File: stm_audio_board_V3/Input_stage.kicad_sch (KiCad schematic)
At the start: 92 parts, among them U4 OP275

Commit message: minor changes
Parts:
- removed D4 (x4), D6 (x4), D8 (x4), D9 (x4): BAT42W-V, Diode_SMD:D_SOD-123, symbol Diode:BAT42W-V

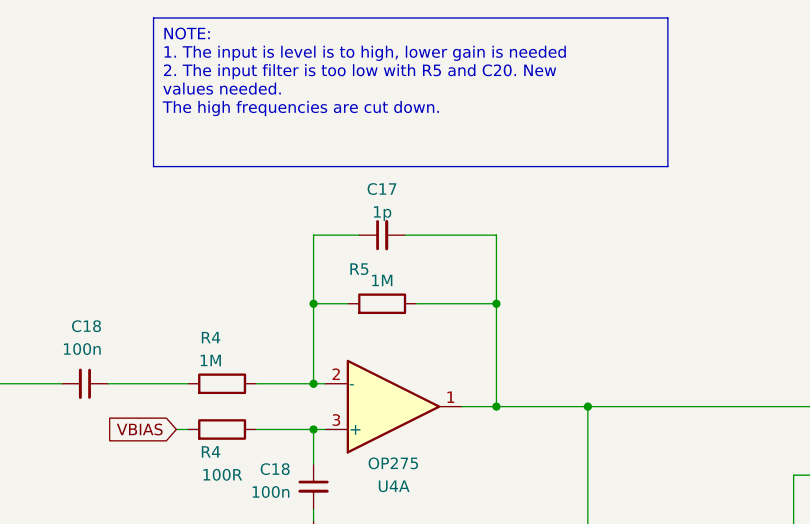
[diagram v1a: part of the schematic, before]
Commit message: Analog power and SDRAm routing reworked
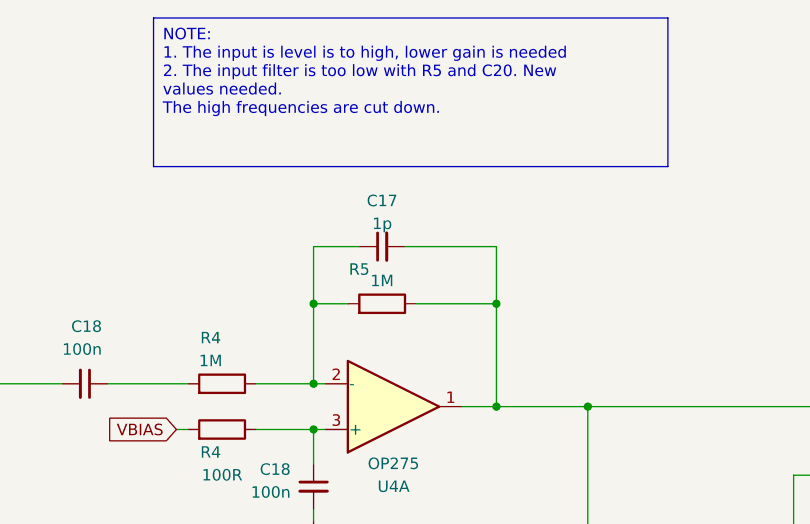
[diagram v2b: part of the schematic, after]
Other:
- moved on the sheet: C17
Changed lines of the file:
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@@
     (stroke (width 0) (type default))
   )
-  (wire (pts (xy 110.49 53.34) (xy 105.41 53.34))
+  (wire (pts (xy 110.49 54.61) (xy 105.41 54.61))
     (stroke (width 0) (type default))
   )
@@
     (stroke (width 0) (type default))
   )
-  (wire (pts (xy 115.57 53.34) (xy 125.73 53.34))
+  (wire (pts (xy 115.57 54.61) (xy 125.73 54.61))
     (stroke (width 0) (type default))
   )
@@
     (stroke (width 0) (type default))
   )
-  (wire (pts (xy 125.73 60.96) (xy 125.73 53.34))
+  (wire (pts (xy 125.73 54.61) (xy 125.73 60.96))
     (stroke (width 0) (type default))
   )
@@
     (stroke (width 0) (type default))
   )
-  (wire (pts (xy 105.41 60.96) (xy 105.41 53.34))
+  (wire (pts (xy 105.41 54.61) (xy 105.41 60.96))
     (stroke (width 0) (type default))
   )
@@
     )
   )
-  (symbol (lib_id "Device:C_Small") (at 113.03 53.34 90) (mirror x) (unit 1)
-    (in_bom yes) (on_board yes) (dnp no)
-    (property "Reference" "C17" (at 113.0363 48.26 90)
-      (effects (font (size 1.27 1.27)))
-    )
-    (property "Value" "1p" (at 113.0363 50.8 90)
-      (effects (font (size 1.27 1.27)))
-    )
-    (property "Footprint" "Capacitor_SMD:C_0603_1608Metric" (at 113.03 53.34 0)
-      (effects (font (size 1.27 1.27)) hide)
-    )
-    (property "Datasheet" "~" (at 113.03 53.34 0)
-      (effects (font (size 1.27 1.27)) hide)
-    )
+  (symbol (lib_id "Device:C_Small") (at 113.03 54.61 90) (mirror x) (unit 1)
+    (in_bom yes) (on_board yes) (dnp no)
+    (property "Reference" "C17" (at 113.0363 49.53 90)
+      (effects (font (size 1.27 1.27)))
+    )
+    (property "Value" "1p" (at 113.0363 52.07 90)
+      (effects (font (size 1.27 1.27)))
+    )
+    (property "Footprint" "Capacitor_SMD:C_0603_1608Metric" (at 113.03 54.61 0)
+      (effects (font (size 1.27 1.27)) hide)
+    )
+    (property "Datasheet" "~" (at 113.03 54.61 0)
+      (effects (font (size 1.27 1.27)) hide)
+    )

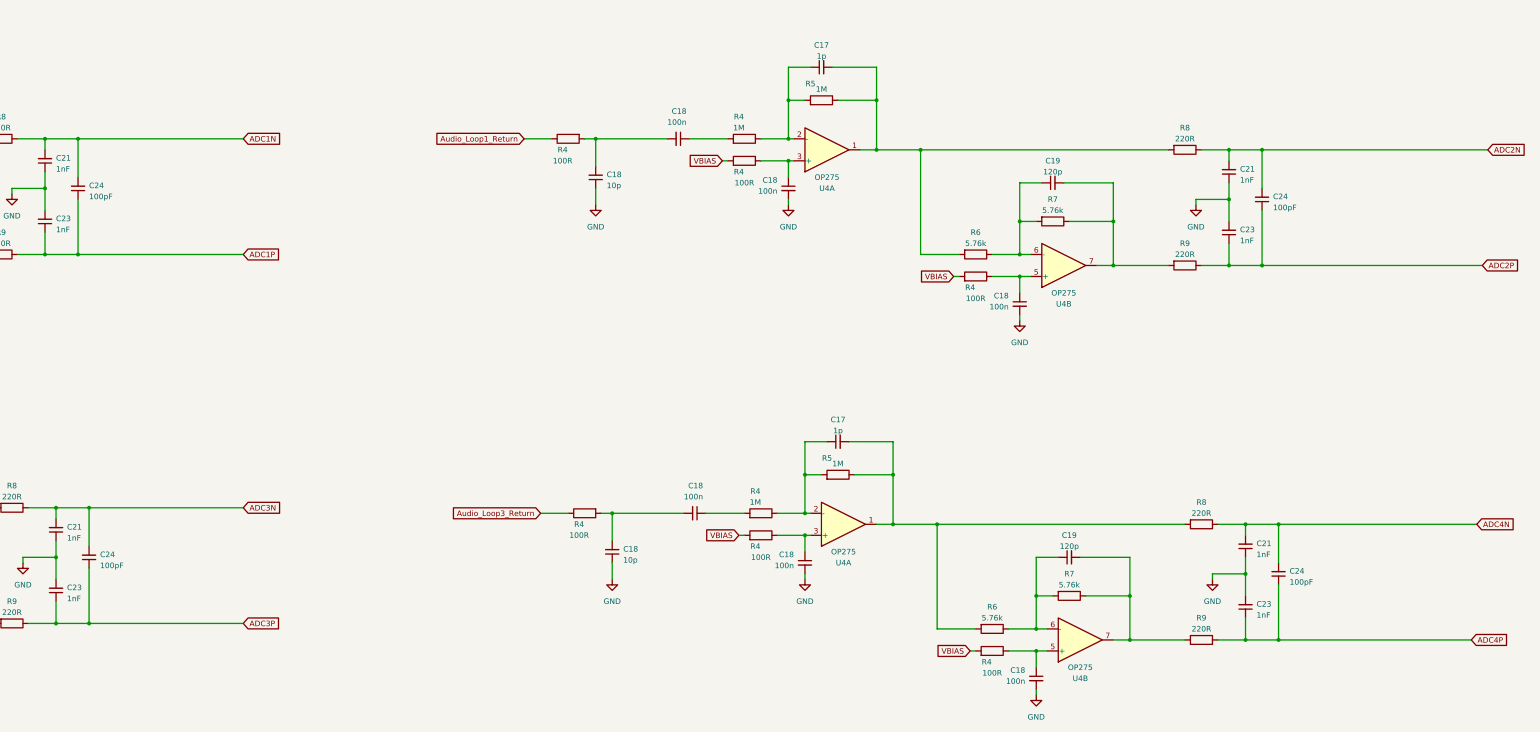
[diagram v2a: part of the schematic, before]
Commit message: New orientation, Overvoltage protection added
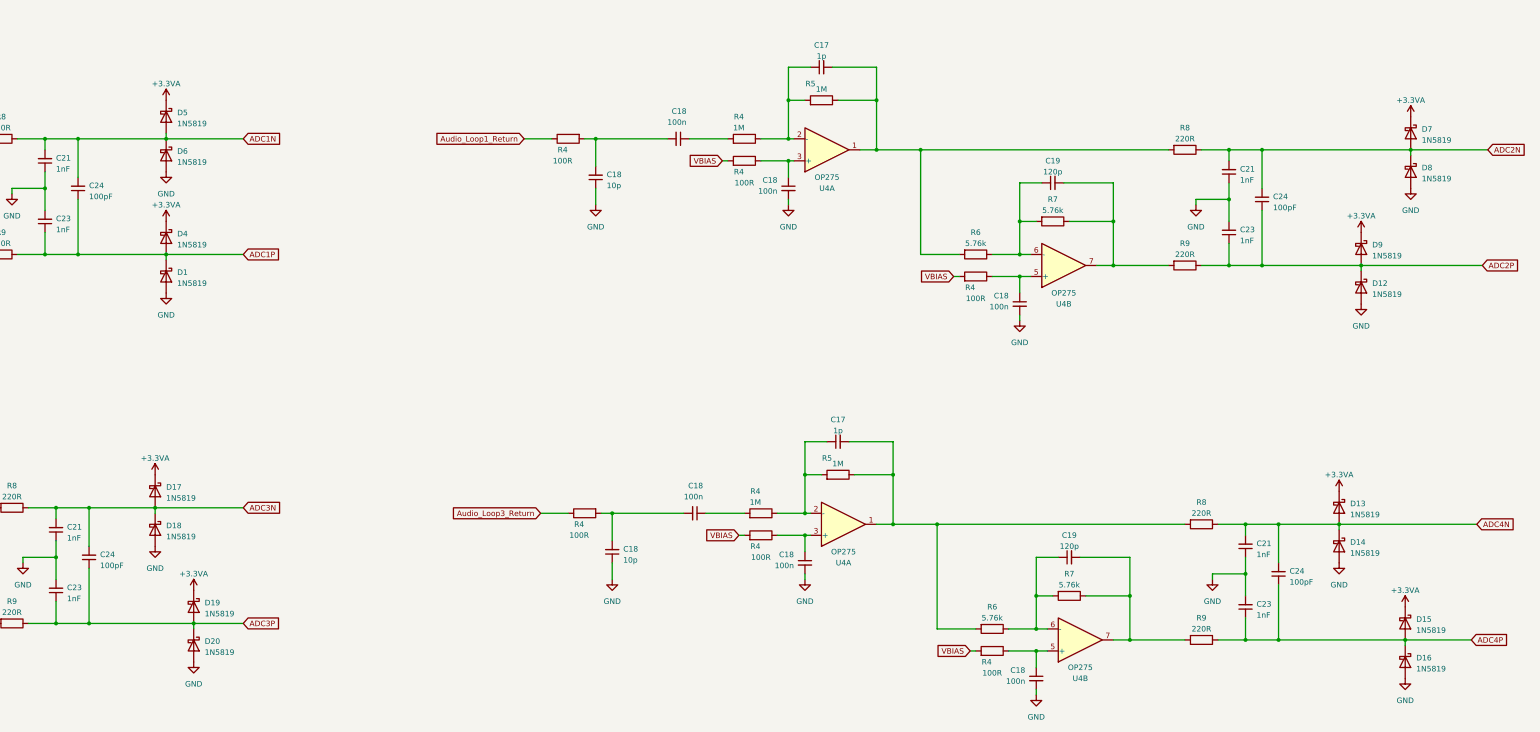
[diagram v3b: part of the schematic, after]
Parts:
- added D1, D12, D13, D14, D15, D16, D17, D18, D19, D20, D4, D5, D6, D7, D8, D9: 1N5819, Diode_SMD:D_SOD-323, symbol Diode:1N5819
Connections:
- net ADC1N: now also D5.2 (A), D6.1 (K)
- net ADC1P: now also D1.1 (K), D4.2 (A)
- net ADC2N: now also D7.2 (A), D8.1 (K)
- net ADC2P: now also D12.1 (K), D9.2 (A)
- net ADC3N: now also D17.2 (A), D18.1 (K)
- net ADC3P: now also D19.2 (A), D20.1 (K)
- net ADC4N: now also D13.2 (A), D14.1 (K)
- net ADC4P: now also D15.2 (A), D16.1 (K)
- net GND: now also D1.2 (A), D12.2 (A), D14.2 (A), D16.2 (A), D18.2 (A), D20.2 (A), D6.2 (A), D8.2 (A)
- new net +3.3VA: D13.1 (K), D15.1 (K), D17.1 (K), D19.1 (K), D4.1 (K), D5.1 (K), D7.1 (K), D9.1 (K)

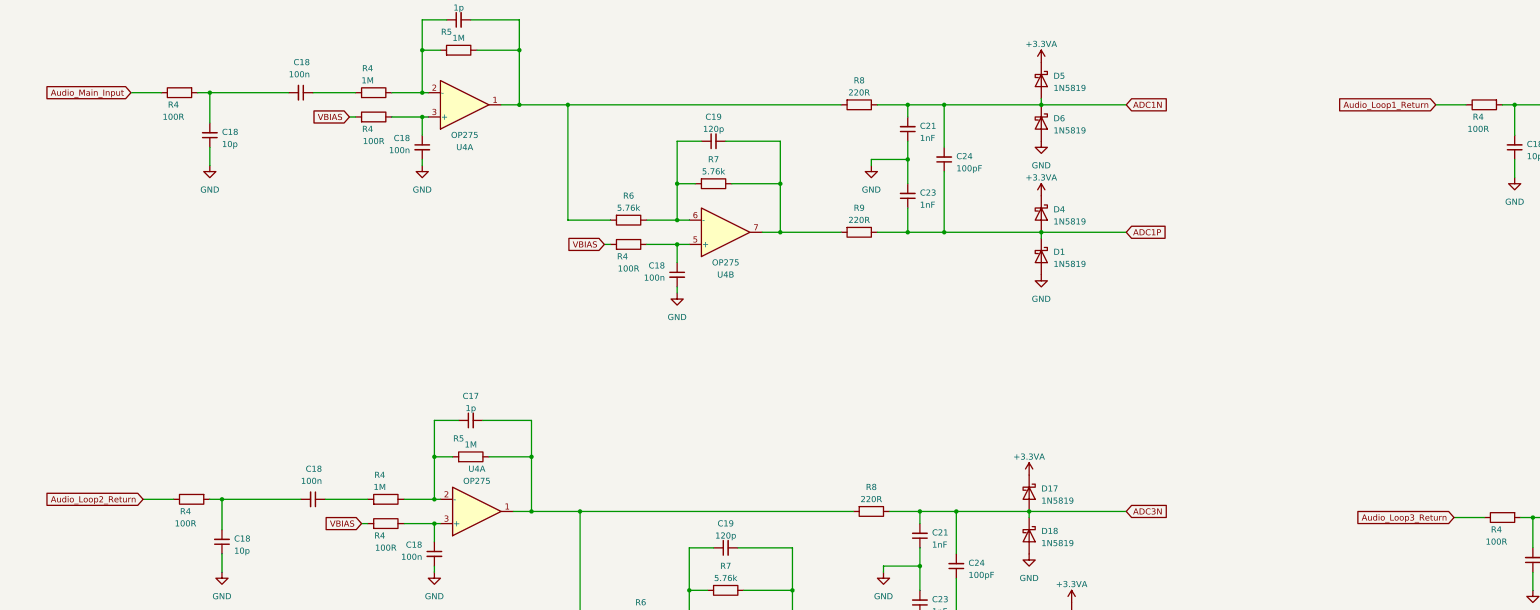
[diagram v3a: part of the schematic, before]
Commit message: Reworked outline for enclosure
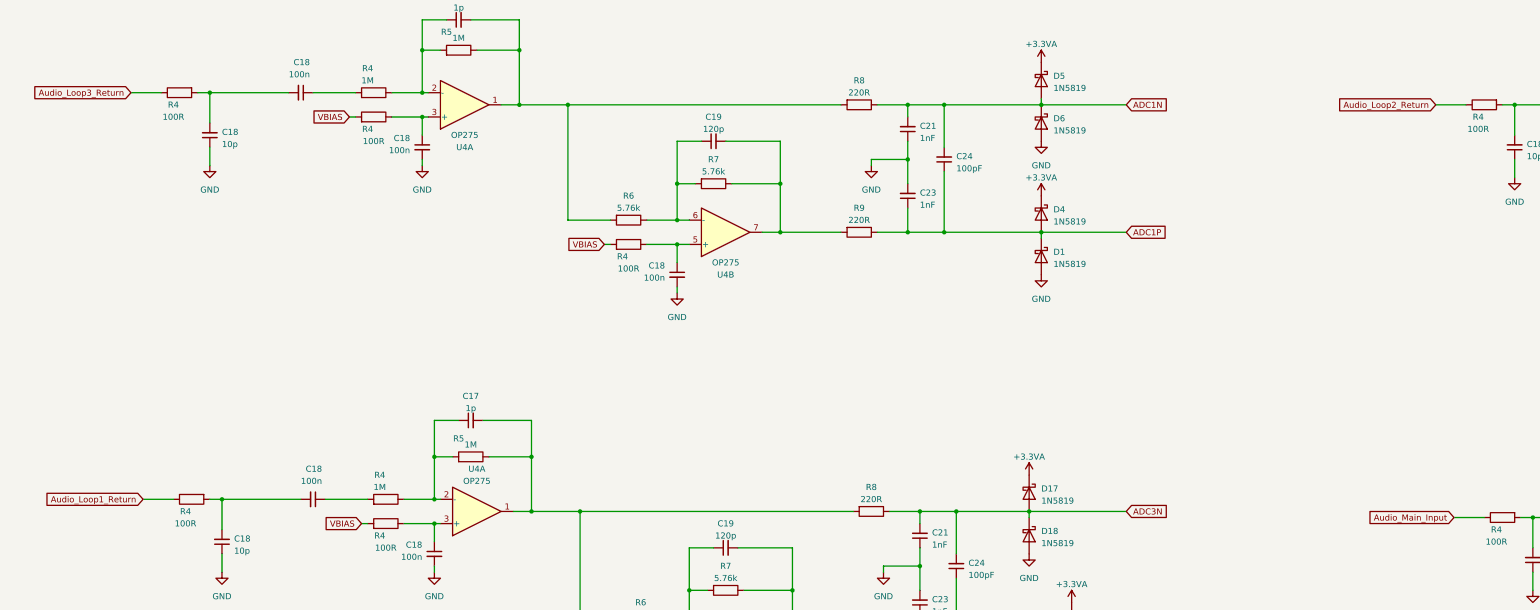
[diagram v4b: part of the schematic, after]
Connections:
- net Audio_Loop1_Return: now also R4.1; no longer R4.1
- net Audio_Loop2_Return: now also R4.1; no longer R4.1
- net Audio_Loop3_Return: now also R4.1; no longer R4.1
- net Audio_Main_Input: now also R4.1; no longer R4.1
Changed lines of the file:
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@@
     (effects (font (size 1.27 1.27)) (justify left top))
-  )
-  (global_label "Audio_Loop2_Return" (shape input) (at 46.99 154.94 180) (fields_autoplaced)
-    (effects (font (size 1.27 1.27)) (justify right))
-    (property "Intersheetrefs" "${INTERSHEET_REFS}" (at 25.1555 154.94 0)
-      (effects (font (size 1.27 1.27)) (justify right) hide)
-    )
   )
   (global_label "ADC1N" (shape input) (at 252.73 72.39 0) (fields_autoplaced)
@@
     )
   )
-  (global_label "Audio_Main_Input" (shape input) (at 44.45 69.85 180) (fields_autoplaced)
-    (effects (font (size 1.27 1.27)) (justify right))
-    (property "Intersheetrefs" "${INTERSHEET_REFS}" (at 25.3369 69.85 0)
-      (effects (font (size 1.27 1.27)) (justify right) hide)
-    )
-  )
   (global_label "ADC4P" (shape input) (at 535.94 187.96 0) (fields_autoplaced)
     (effects (font (size 1.27 1.27)) (justify left))
     (property "Intersheetrefs" "${INTERSHEET_REFS}" (at 544.9539 187.96 0)
       (effects (font (size 1.27 1.27)) (justify left) hide)
+    )
+  )
+  (global_label "Audio_Main_Input" (shape input) (at 321.31 158.75 180) (fields_autoplaced)
+    (effects (font (size 1.27 1.27)) (justify right))
+    (property "Intersheetrefs" "${INTERSHEET_REFS}" (at 302.1969 158.75 0)
+      (effects (font (size 1.27 1.27)) (justify right) hide)
     )
   )
@@
     )
   )
-  (global_label "Audio_Loop3_Return" (shape input) (at 321.31 158.75 180) (fields_autoplaced)
+  (global_label "Audio_Loop3_Return" (shape input) (at 44.45 69.85 180) (fields_autoplaced)
     (effects (font (size 1.27 1.27)) (justify right))
-    (property "Intersheetrefs" "${INTERSHEET_REFS}" (at 299.4755 158.75 0)
+    (property "Intersheetrefs" "${INTERSHEET_REFS}" (at 22.6155 69.85 0)
       (effects (font (size 1.27 1.27)) (justify right) hide)
     )
@@
     (property "Intersheetrefs" "${INTERSHEET_REFS}" (at 547.4939 101.6 0)
       (effects (font (size 1.27 1.27)) (justify left) hide)
-    )
-  )
-  (global_label "Audio_Loop1_Return" (shape input) (at 317.5 72.39 180) (fields_autoplaced)
-    (effects (font (size 1.27 1.27)) (justify right))
-    (property "Intersheetrefs" "${INTERSHEET_REFS}" (at 295.6655 72.39 0)
-      (effects (font (size 1.27 1.27)) (justify right) hide)
     )
   )
@@
     )
   )
+  (global_label "Audio_Loop2_Return" (shape input) (at 317.5 72.39 180) (fields_autoplaced)
+    (effects (font (size 1.27 1.27)) (justify right))
+    (property "Intersheetrefs" "${INTERSHEET_REFS}" (at 295.6655 72.39 0)
+      (effects (font (size 1.27 1.27)) (justify right) hide)
+    )
+  )
   (global_label "VBIAS" (shape input) (at 367.03 163.83 180) (fields_autoplaced)
     (effects (font (size 1.27 1.27)) (justify right))
@@
       (effects (font (size 1.27 1.27)) (justify right) hide)
     )
+  )
+  (global_label "Audio_Loop1_Return" (shape input) (at 46.99 154.94 180) (fields_autoplaced)
+    (effects (font (size 1.27 1.27)) (justify right))
+    (property "Intersheetrefs" "${INTERSHEET_REFS}" (at 25.1555 154.94 0)
+      (effects (font (size 1.27 1.27)) (justify right) hide)
+    )
